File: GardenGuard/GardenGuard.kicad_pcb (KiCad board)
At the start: 2 copper layers, 40 x 99.5 mm, 68 parts, among them J1 Sollar, J2 OLED SSD1306, J3 AudioJack4_Ground_SwitchTR1, J4 USB_B_Mini, J5 Conn_01x07, J6 Conn_01x02, Q1 BC847B, Q2 BC847B, Q3 Q_PMOS_DGS, SW1 Reset, SW2 SW_Push, SW3 Rotary_Encoder_Switch, SW4 SW_Push, SW5 SW_Push, U1 ESP-07, U2 DS18B20, U3 CP2104, U4 TP4056, U5 FS8205A, U6 DW01A, U7 LM1117-3.3

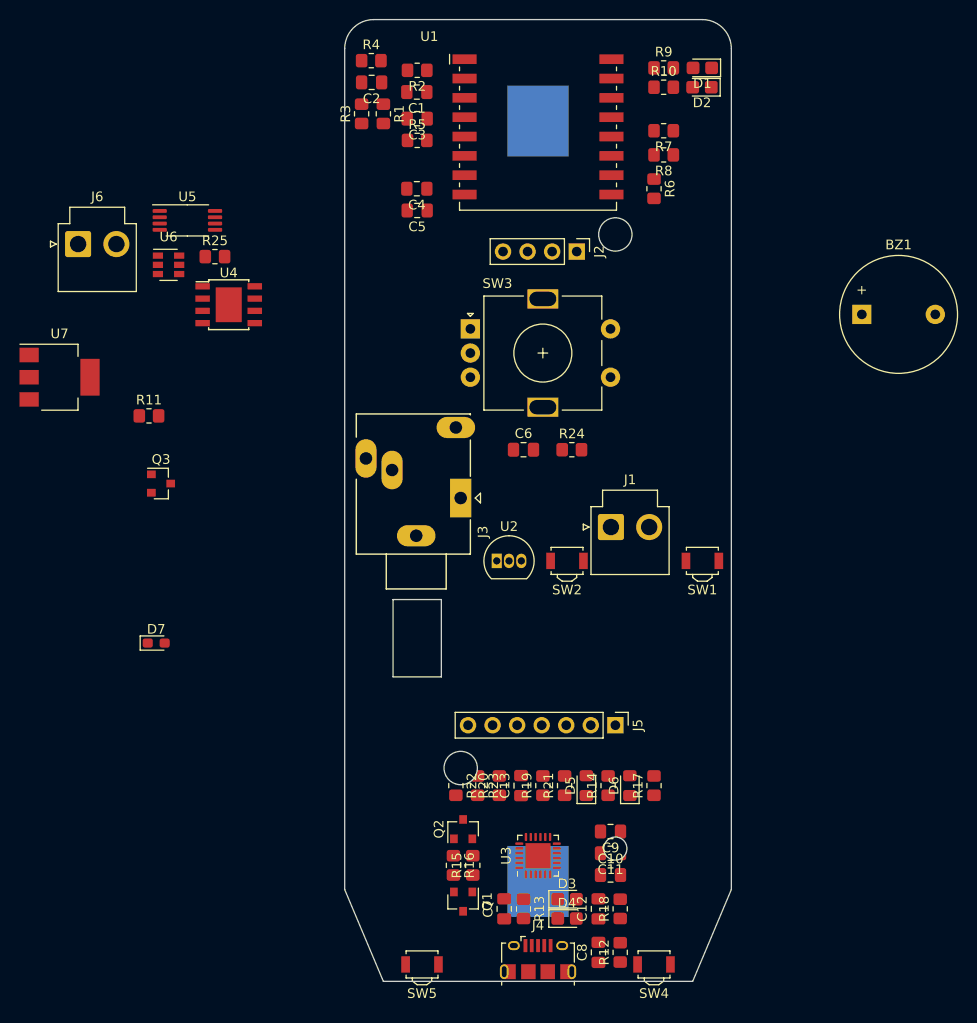
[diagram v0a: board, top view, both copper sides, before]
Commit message: Updated packages, start layout
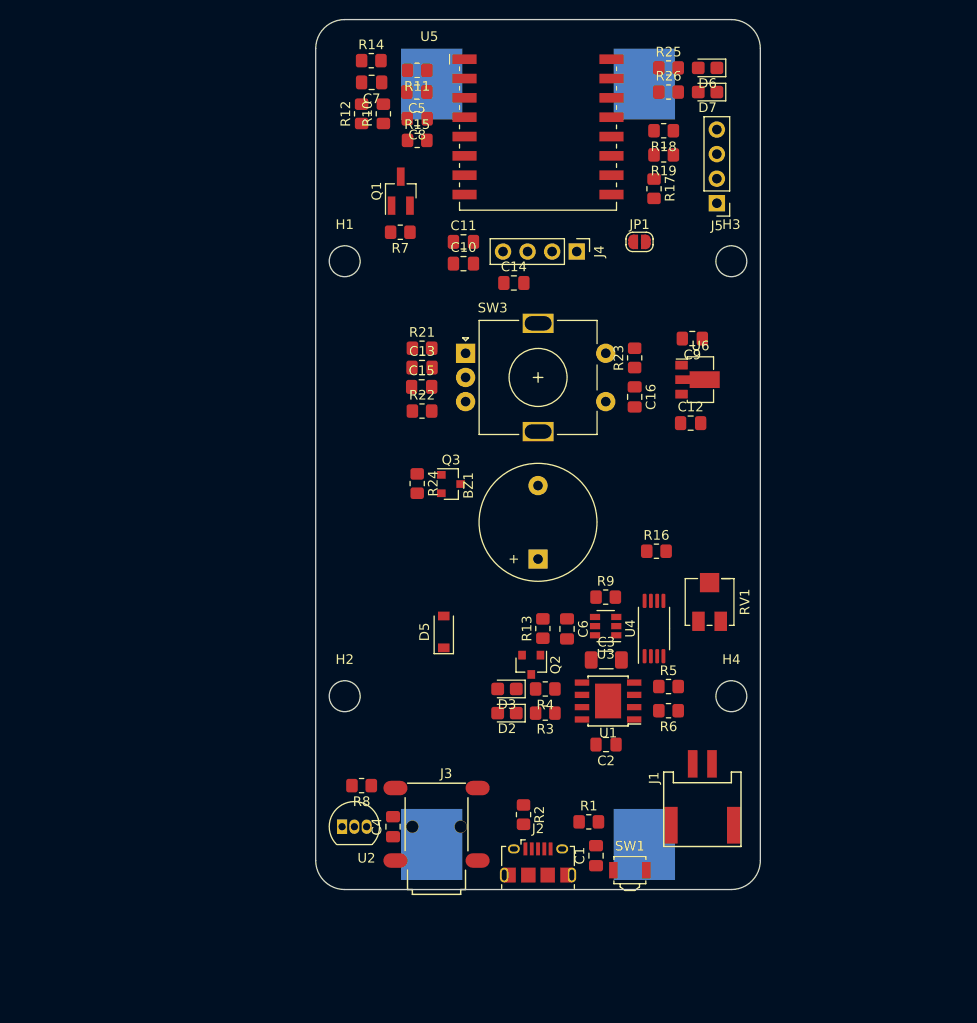
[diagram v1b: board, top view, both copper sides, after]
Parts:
- removed the C10 at (127.5, 148.5)
- removed the C11 at (127.5, 146.2)
- removed the C7 at (116.5, 152.0)
- removed the C8 at (126.2, 156.5)
- removed D4: D_TVS, Diode_SMD:D_0805_2012Metric_Castellated
- removed the D6 at (129.5, 139.2)
- removed the D7 at (80.5, 124.5)
- removed the J4 at (120.0, 157.2)
- removed J6: Conn_01x02, Connector_JST:JST_VH_B2P-VH-B_1x02_P3.96mm_Vertical
- removed the Q2 at (112.2, 143.8)
- removed the R11 at (79.8, 101.0)
- removed the R12 at (128.5, 156.5)
- removed the R14 at (127.2, 139.2)
- removed the R15 at (113.2, 147.5)
- removed the R16 at (111.2, 147.5)
- removed the R17 at (132.0, 139.2)
- removed the R18 at (128.5, 152.0)
- removed the R19 at (120.5, 139.2)
- removed R20: 10k, Resistor_SMD:R_0805_2012Metric_Pad1.20x1.40mm_HandSolder
- removed SW2, SW4, SW5: SW_Push, Button_Switch_SMD:SW_SPST_B3U-3000P
- removed the U3 at (120.0, 146.5)
- removed U7: LM1117-3.3, Package_TO_SOT_SMD:SOT-223
- added BT1: LiOn, Battery:BatteryHolder_Keystone_1042_1x18650, B.Cu at (131.0, 106.0)
- added C1: 10n, Capacitor_SMD:C_0805_2012Metric_Pad1.18x1.45mm_HandSolder, F.Cu at (126.0, 146.5)
- added C14: 0.1uF, Capacitor_SMD:C_0805_2012Metric_Pad1.18x1.45mm_HandSolder, F.Cu at (117.5, 87.2)
- added C15: 10nF, Capacitor_SMD:C_0805_2012Metric_Pad1.18x1.45mm_HandSolder, F.Cu at (108.0, 98.0)
- added C16: 10nF, Capacitor_SMD:C_0805_2012Metric_Pad1.18x1.45mm_HandSolder, F.Cu at (130.0, 99.0)
- added C2: 0.1uF, Capacitor_SMD:C_0805_2012Metric_Pad1.18x1.45mm_HandSolder, F.Cu at (127.0, 135.0)
- added C3: 10uF, Capacitor_SMD:C_1206_3216Metric_Pad1.33x1.80mm_HandSolder, F.Cu at (127.1, 126.2)
- added C6: 0.1uF, Capacitor_SMD:C_0805_2012Metric_Pad1.18x1.45mm_HandSolder, F.Cu at (123.0, 123.0)
- added D2: R, LED_SMD:LED_0805_2012Metric_Castellated, F.Cu at (116.8, 131.8)
- added H1: MountingHole, MountingHole:MountingHole_3.2mm_M3_DIN965, F.Cu at (100.0, 85.0)
- added H2: MountingHole, MountingHole:MountingHole_3.2mm_M3_DIN965, F.Cu at (100.0, 130.0)
- added H3: MountingHole, MountingHole:MountingHole_3.2mm_M3_DIN965, F.Cu at (140.0, 85.0)
- added H4: MountingHole, MountingHole:MountingHole_3.2mm_M3_DIN965, F.Cu at (140.0, 130.0)
- added J2: USB_B_Mini, Connector_USB:USB_Micro-B_Amphenol_10118194_Horizontal, F.Cu at (120.0, 147.2)
- added JP1: BOOT, Jumper:SolderJumper-2_P1.3mm_Open_RoundedPad1.0x1.5mm, F.Cu at (130.5, 83.0)
- added Q3: BC548, Package_TO_SOT_SMD:SOT-23, F.Cu at (111.0, 108.0)
- added R1: 1M, Resistor_SMD:R_0805_2012Metric_Pad1.20x1.40mm_HandSolder, F.Cu at (125.2, 143.0)
- added R2: 0R, Resistor_SMD:R_0805_2012Metric_Pad1.20x1.40mm_HandSolder, F.Cu at (118.5, 142.2)
- added R24: 10K, Resistor_SMD:R_0805_2012Metric_Pad1.20x1.40mm_HandSolder, F.Cu at (107.5, 108.0)
- added R3: 1K, Resistor_SMD:R_0805_2012Metric_Pad1.20x1.40mm_HandSolder, F.Cu at (120.8, 131.8)
- added R4: 1K, Resistor_SMD:R_0805_2012Metric_Pad1.20x1.40mm_HandSolder, F.Cu at (120.8, 129.2)
- added R5: 1K, Resistor_SMD:R_0805_2012Metric_Pad1.20x1.40mm_HandSolder, F.Cu at (133.5, 129.0)
- added R6: 1K, Resistor_SMD:R_0805_2012Metric_Pad1.20x1.40mm_HandSolder, F.Cu at (133.5, 131.5)
- added R7: 100K, Resistor_SMD:R_0805_2012Metric_Pad1.20x1.40mm_HandSolder, F.Cu at (105.8, 82.0)
- added R9: 1K, Resistor_SMD:R_0805_2012Metric_Pad1.20x1.40mm_HandSolder, F.Cu at (127.0, 119.8)
- added RV1: 10K, Potentiometer_SMD:Potentiometer_Bourns_3224J_Horizontal, F.Cu at (137.8, 120.2)
- added U6: HT75xx-1-SOT89, Package_TO_SOT_SMD:SOT-89-3, F.Cu at (136.5, 97.2)
- BT2: renamed from BT1; value Battery_Cell -> LiOn
- C12, C9: value 100nF -> 10uF
- C13: value 4.7uF -> 10nF
- D3: value D_TVS -> B; footprint Diode_SMD:D_0805_2012Metric_Castellated -> LED_SMD:LED_0805_2012Metric_Castellated
- D5: value R -> 1N5819; footprint LED_SMD:LED_0805_2012Metric_Pad1.15x1.40mm_HandSolder -> Diode_SMD:D_SOD-123
- J1: footprint Connector_JST:JST_VH_B2P-VH-B_1x02_P3.96mm_Vertical -> Project_footprints:ER-CON2.0-2P-SMD
- J3: value AudioJack4_Ground_SwitchTR1 -> PJ-321A; footprint Connector_Audio:Jack_3.5mm_Ledino_KB3SPRS_Horizontal -> Project_footprints:PJ-321A
- J5: value Conn_01x07 -> DEBUG; footprint Connector_PinHeader_2.54mm:PinHeader_1x07_P2.54mm_Vertical -> Connector_PinHeader_2.54mm:PinHeader_1x04_P2.54mm_Vertical
- Q1: value BC847B -> RE1C002UN; footprint Package_TO_SOT_SMD:SOT-23 -> Package_TO_SOT_SMD:SOT-23_Handsoldering
- Q2: renamed from Q3; value Q_PMOS_DGS -> FQP27P06
- R10: renamed from R1; value 220k -> 220K
- R11: renamed from R2; value 100k -> 100K
- R12: renamed from R3; value 100k -> 1K
- R13: value 0R -> 100R
- R14: renamed from R4; value 100k -> 100K
- R15: renamed from R5; value 100k -> 100K
- R18: renamed from R7; value 100k -> 100K
- R21: value 4.7k -> 10K
- R22, R23: value 100R -> 10K
- moved Q1 73.8 mm to (105.8, 77.8), turned to 90 degrees
- moved U4 64.1 mm to (132.0, 123.0), turned to 90 degrees
- moved U3 58.7 mm to (127.0, 122.8), turned to 180 degrees
- moved U1 56.8 mm to (127.2, 130.5), turned to 180 degrees
- moved J5 55.0 mm to (138.5, 79.0), turned to 180 degrees
- moved R16 54.9 mm to (132.2, 115.0)
- moved C9 51.7 mm to (136.0, 93.0)
- moved C12 51.1 mm to (135.8, 101.8), turned to 0 degrees
- moved R21 47.6 mm to (108.0, 94.0), turned to 0 degrees
- moved R23 47.1 mm to (130.0, 95.0), turned to 90 degrees
- moved C13 44.4 mm to (108.0, 96.0), turned to 0 degrees
- moved Q2 42.6 mm to (119.3, 126.8), turned to 270 degrees
- moved C4 41.3 mm to (105.0, 143.5), turned to 90 degrees
- moved J3 41.1 mm to (109.5, 150.5)
- moved R8 41.0 mm to (101.8, 139.2), turned to 180 degrees
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- renumbered C4 to C10, C5 to C11, C6 to C4, C1 to C5, C2 to C7, C3 to C8, D1 to D6, D2 to D7, J2 to J4, R25 to R16, R6 to R17, R8 to R19, R9 to R25, R10 to R26, R24 to R8, U4 to U1, U6 to U3, U5 to U4, U1 to U5
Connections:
- net /GPIO15 renamed /BUZZ
- BT2 pad 1: (no net) -> V_BAT
- BT2 pad 2: (no net) -> GND1
- BZ1 pad 1: (no net) -> +3V3
- BZ1 pad 2: (no net) -> Net-(BZ1-Pad2)
- C12 pad 1: GND -> +3V3
- C12 pad 2: V_IO -> GND
- C13 pad 1: Net-(C13-Pad1) -> /GPIO13
- C9 pad 1: GND -> Net-(C9-Pad1)
- C9 pad 2: VBUS -> GND
- D3 pad 2: /programmer/SHIELD -> VCC
- D5 pad 1: Net-(D5-Pad1) -> Net-(C9-Pad1)
- D5 pad 2: Net-(D5-Pad2) -> VCC
- J1 pad 1: (no net) -> VCC
- J1 pad 2: (no net) -> GND
- J5 pad 1: VDD -> +3V3
- J5 pad 2: V_IO -> /RXD
- J5 pad 3: /programmer/TXD -> /TXD
- J5 pad 4: /programmer/RXD -> GND
- Q1 pad 1: Net-(Q1-Pad1) -> B_CHECK
- Q1 pad 2: RST -> V_BAT
- Q1 pad 3: /programmer/EN -> Net-(Q1-Pad3)
- Q2 pad 1: (no net) -> V_BAT
- Q2 pad 2: (no net) -> VCC
- Q2 pad 3: (no net) -> Net-(C9-Pad1)
- R10 pad 1: /ADC1 -> Net-(Q1-Pad3)
- R10 pad 2: (no net) -> /ADC1
- R13 pad 1: VBUS -> V_BAT
- R13 pad 2: Net-(J4-Pad1) -> Net-(C6-Pad1)
- R16 pad 1: (no net) -> VCC
- R16 pad 2: (no net) -> GND
- R21 pad 1: Net-(R21-Pad1) -> /GPIO13
- R21 pad 2: V_IO -> Net-(R21-Pad2)
- R22 pad 1: /programmer/TXD -> /GPIO14
- R23 pad 1: /programmer/RXD -> /GPIO0
- R25 pad 1: /GPIO14 -> /GPIO2
- R26 pad 1: /GPIO14 -> /GPIO2
- SW3 pad A: (no net) -> Net-(R21-Pad2)
- SW3 pad B: (no net) -> Net-(R22-Pad2)
- SW3 pad C: (no net) -> GND
- SW3 pad S1: (no net) -> GND
- SW3 pad S2: (no net) -> Net-(R23-Pad2)
- U1 pad 1: (no net) -> Net-(U1-Pad1)
- U1 pad 2: (no net) -> Net-(R5-Pad1)
- U1 pad 3: (no net) -> GND
- U1 pad 4: (no net) -> VCC
- U1 pad 5: (no net) -> V_BAT
- U1 pad 6: (no net) -> Net-(R4-Pad1)
- U1 pad 7: (no net) -> Net-(R3-Pad1)
- U1 pad 8: (no net) -> VCC
- U3 pad 1: (no net) -> Net-(U3-Pad1)
- U3 pad 2: (no net) -> Net-(R9-Pad1)
- U3 pad 3: (no net) -> Net-(U3-Pad3)
- U3 pad 4: (no net) -> Net-(U3-Pad4)
- U3 pad 5: (no net) -> Net-(C6-Pad1)
- U3 pad 6: (no net) -> GND1
- U4 pad 1: (no net) -> Net-(U4-Pad1)
- U4 pad 2: (no net) -> GND1
- U4 pad 3: (no net) -> GND1
- U4 pad 4: (no net) -> Net-(U3-Pad1)
- U4 pad 5: (no net) -> Net-(U3-Pad3)
- U4 pad 6: (no net) -> GND
- U4 pad 7: (no net) -> GND
- U4 pad 8: (no net) -> Net-(U4-Pad8)
- U5 pad 15: (no net) -> /RXD
- U5 pad 16: (no net) -> /TXD
- U5 pad 6: (no net) -> B_CHECK
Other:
- board size 40 x 99.5 mm -> 46 x 90 mm
- net class Power added: clearance 0.2, trace_width 0.25, via_dia 0.8, via_drill 0.4
- net class Signal added: clearance 0.2, trace_width 0.25, via_dia 0.8, via_drill 0.4

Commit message: layout done
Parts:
- added C17: 0.1uF, Capacitor_SMD:C_1206_3216Metric_Pad1.33x1.80mm_HandSolder, F.Cu at (139.2, 109.5)
- C10, C2: footprint Capacitor_SMD:C_0805_2012Metric_Pad1.18x1.45mm_HandSolder -> Capacitor_SMD:C_1206_3216Metric_Pad1.33x1.80mm_HandSolder
- Q2: footprint Package_TO_SOT_SMD:SOT-23 -> Package_TO_SOT_SMD:SOT-23_Handsoldering
- Q3: value BC548 -> Q_NPN_BEC; footprint Package_TO_SOT_SMD:SOT-23 -> Package_TO_SOT_SMD:SOT-23_Handsoldering
- moved D5 29.7 mm to (136.5, 109.5), turned to 270 degrees
- moved RV1 21.7 mm to (121.0, 134.0), turned to 0 degrees
- moved Q2 21.4 mm to (132.0, 109.5), turned to 180 degrees
- moved R13 12.4 mm to (128.5, 113.5), turned to 270 degrees
- moved C9 12.0 mm to (137.0, 105.0), turned to 0 degrees
- moved R5 8.60 mm to (126.5, 134.0), turned to 270 degrees
- moved C2 8.18 mm to (132.0, 128.5), turned to 270 degrees
- moved C6 7.80 mm to (128.5, 117.5)
- moved JP1 7.62 mm to (124.3, 87.5), turned to 180 degrees
- moved U3 7.60 mm to (132.5, 117.5)
- moved U4 7.43 mm to (137.0, 117.5)
- moved J5 7.00 mm to (138.5, 72.0), turned to 0 degrees
- moved C1 6.95 mm to (122.5, 140.5), turned to 180 degrees
- moved R3 6.79 mm to (121.5, 125.0), turned to 270 degrees
- moved R12 5.80 mm to (102.5, 64.0), turned to 0 degrees
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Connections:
- net Net-(C6-Pad1) renamed /dw01a_vcc
- net Net-(R5-Pad1) renamed /prog
- net Net-(R9-Pad1) renamed /dw01a_cs
- net Net-(U1-Pad1) renamed /T_BAT
- net Net-(U3-Pad1) renamed /dw01a_od
- net Net-(U3-Pad3) renamed /dw01a_oc
- C15 pad 1: /GPIO14 -> /GPIO12
- J1 pad 1: VCC -> GND
- J1 pad 2: GND -> VCC
- J3 pad 3: /GPIO13 -> /GPIO12
- Q2 pad 1: V_BAT -> VCC
- Q2 pad 2: VCC -> Net-(C9-Pad1)
- Q2 pad 3: Net-(C9-Pad1) -> V_BAT
- Q3 pad 1: Net-(BZ1-Pad2) -> Net-(Q3-Pad1)
- Q3 pad 2: Net-(Q3-Pad2) -> GND
- Q3 pad 3: GND -> Net-(BZ1-Pad2)
- R22 pad 1: /GPIO14 -> /GPIO12
- R24 pad 2: Net-(Q3-Pad2) -> Net-(Q3-Pad1)
- R8 pad 2: /GPIO13 -> /GPIO12
- U2 pad 2: /GPIO13 -> /GPIO12
- U5 pad 5: /GPIO14 -> B_CHECK
- U5 pad 6: B_CHECK -> /GPIO12
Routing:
- net +3V3: track 0.00 -> 203.9 mm, vias 0 -> 5
- net /Reset: track 0.00 -> 118.7 mm, vias 0 -> 2
- net V_BAT: track 0.00 -> 104.4 mm, vias 0 -> 4
- net VCC: track 0.00 -> 101.5 mm, vias 0 -> 2
- net /GPIO12: track 0.00 -> 98.3 mm
- net GND1: track 0.00 -> 80.5 mm, vias 0 -> 5
- net /BUZZ: track 0.00 -> 53.1 mm, vias 0 -> 2
- net /GPIO13: track 0.00 -> 50.7 mm
- net /GPIO0: track 0.00 -> 39.1 mm
- net GND: track 0.00 -> 38.2 mm, vias 0 -> 127
- net /TXD: track 0.00 -> 27.6 mm
- net /RXD: track 0.00 -> 24.6 mm
- net WAKE: track 0.00 -> 22.2 mm
- net /GPIO2: track 0.00 -> 20.2 mm
- net SCL: track 0.00 -> 19.1 mm
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- added copper zone on B.Cu, net GND
- added copper zone on F.Cu, net GND
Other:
- net class Default: clearance 0.2 -> 0.3; trace_width 0.25 -> 0.3; via_dia 0.8 -> 0.6
- net class Power: clearance 0.2 -> 0.3; trace_width 0.25 -> 0.8; via_drill 0.4 -> 0.6
- net class Signal: clearance 0.2 -> 0.3; trace_width 0.25 -> 0.3; via_dia 0.8 -> 0.6
- rule trace_clearance: 0.2 -> 0.3
- board text added: "GardenGuard"

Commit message: Release v1.0.0 - board finished
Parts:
- added R20: 0R, Resistor_SMD:R_0805_2012Metric_Pad1.20x1.40mm_HandSolder, F.Cu at (135.0, 135.8)
- added R27: 1K, Resistor_SMD:R_0805_2012Metric_Pad1.20x1.40mm_HandSolder, F.Cu at (115.2, 127.8)
- added R28: 1K, Resistor_SMD:R_0805_2012Metric_Pad1.20x1.40mm_HandSolder, F.Cu at (115.2, 132.0)
- added REF**: WEEE-Logo_4.2x6mm_SilkScreen, Symbol:WEEE-Logo_4.2x6mm_SilkScreen, F.Cu at (132.0, 85.0)
- added REF**: KiCad-Logo2_5mm_SilkScreen, Symbol:KiCad-Logo2_5mm_SilkScreen, F.Cu at (105.8, 126.8)
- added REF**: OSHW-Logo2_9.8x8mm_SilkScreen, Symbol:OSHW-Logo2_9.8x8mm_SilkScreen, F.Cu at (109.5, 134.8)
- added REF**: ESD-Logo_6.6x6mm_SilkScreen, Symbol:ESD-Logo_6.6x6mm_SilkScreen, F.Cu at (101.5, 105.2)
- added TH1: Thermistor_NTC, Resistor_THT:R_Axial_DIN0204_L3.6mm_D1.6mm_P5.08mm_Horizontal, B.Cu at (119.8, 130.6)
- moved D2 1.50 mm to (121.5, 127.5)
- moved D3 1.50 mm to (118.0, 127.5)
- moved R3 1.50 mm to (121.5, 123.5)
- moved R4 1.50 mm to (118.0, 123.5)
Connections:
- J1 pad 2: VCC -> Net-(J1-Pad2)
- U1 pad 9: (no net) -> GND
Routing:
- net /T_BAT: track 0.00 -> 12.9 mm
- net VCC: track 101.5 -> 94.4 mm
- net Net-(J1-Pad2): track 0.00 -> 2.80 mm
- net Net-(R4-Pad1): track 12.8 -> 13.5 mm
- net GND: vias 127 -> 129
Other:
- outline, holes or cut-outs redrawn
- board text added: "Aug 2021, Rev 1.0.0"
- board text added: "By: j74a8g@gmail.com github.com/juraj8"

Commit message: Release v1.1.0 - update component values - cleanup
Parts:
- removed REF**: WEEE-Logo_4.2x6mm_SilkScreen, Symbol:WEEE-Logo_4.2x6mm_SilkScreen
- removed REF**: KiCad-Logo2_5mm_SilkScreen, Symbol:KiCad-Logo2_5mm_SilkScreen
- removed REF**: OSHW-Logo2_9.8x8mm_SilkScreen, Symbol:OSHW-Logo2_9.8x8mm_SilkScreen
- removed REF**: ESD-Logo_6.6x6mm_SilkScreen, Symbol:ESD-Logo_6.6x6mm_SilkScreen
- Q1: value RE1C002UN -> IRLML6302
- Q3: value Q_NPN_BEC -> BC850C
- R10: value 220K -> 240k
- R11: value 100K -> 75k
- R12: value 1K -> 91R
- R6: value 1K -> NC
- R7: value 100K -> 1M
- moved J1 0.05 mm to (136.0, 140.9)
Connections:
- J2 pad 2: Net-(J2-Pad2) -> unconnected-(J2-Pad2)
- J2 pad 3: Net-(J2-Pad3) -> unconnected-(J2-Pad3)
- J2 pad 4: Net-(J2-Pad4) -> unconnected-(J2-Pad4)
- U1 pad 9: GND -> (no net)
- U3 pad 4: Net-(U3-Pad4) -> unconnected-(U3-Pad4)
- U4 pad 1: Net-(U4-Pad1) -> unconnected-(U4-Pad1)
- U4 pad 8: Net-(U4-Pad8) -> unconnected-(U4-Pad8)
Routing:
- net /GPIO13: track 50.7 -> 23.0 mm
- net +3V3: track 203.9 -> 210.1 mm
- net Net-(C9-Pad1): track 12.1 -> 7.32 mm
- net GND1: track 80.5 -> 84.3 mm
- net /BUZZ: track 53.1 -> 55.2 mm
- net /TXD: track 27.6 -> 28.5 mm
- net /Reset: track 118.7 -> 119.5 mm
- net /dw01a_cs: track 5.40 -> 5.90 mm
- net GND: vias 129 -> 135
- net (no net): vias 1 -> 0
- added copper zone on F.Cu, net Net-(C9-Pad1)
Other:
- net class Default removed
- net class Power removed
- net class Signal removed
- board text added: "${DATE_SHORT}, Rev ${REVISION}"
- board text added: "+ -"
- board text added: "3.3V RXD TXD GND"
- board text removed: "Aug 2021, Rev 1.0.0"
